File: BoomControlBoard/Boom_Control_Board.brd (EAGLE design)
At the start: 82.5 x 50.8 mm, 44 parts, among them J1 Servo, J2 FTDI, U1 ATMEGA328P, U2 3.3V/150mA, Y1 16MHz

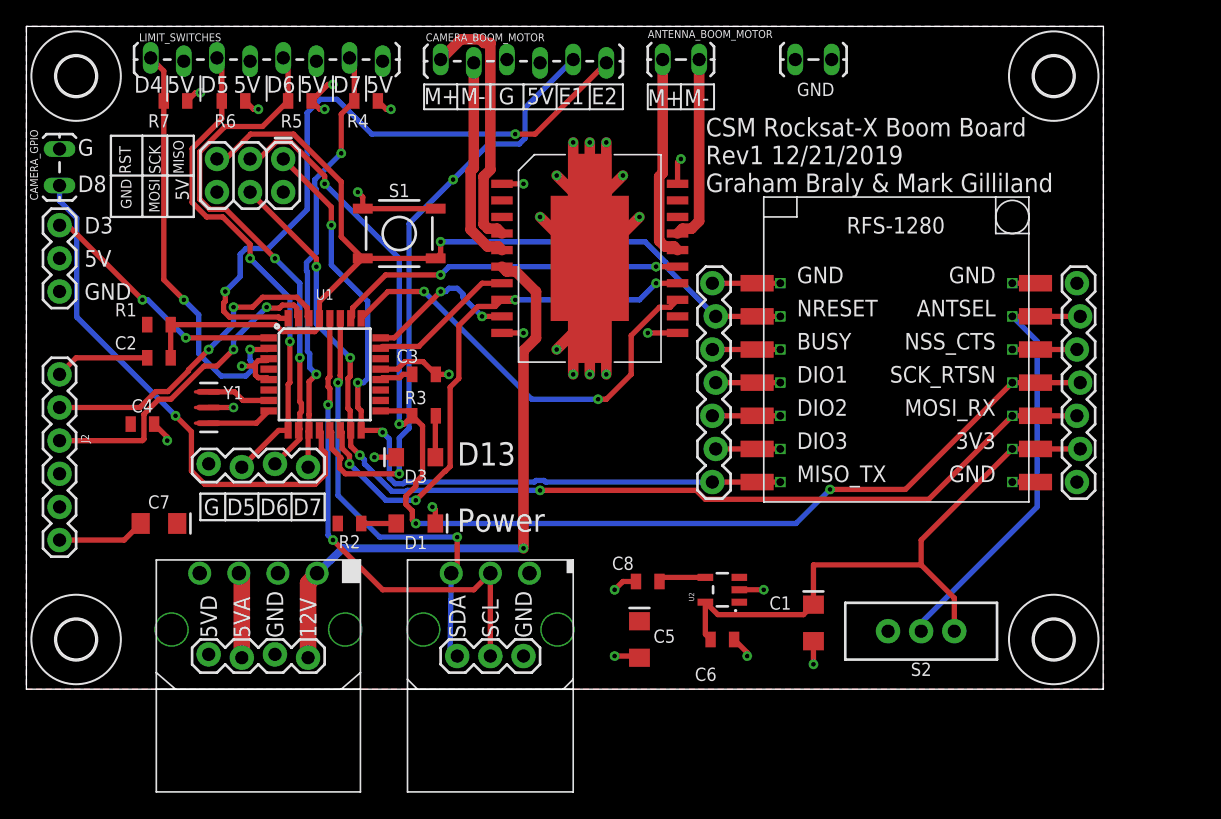
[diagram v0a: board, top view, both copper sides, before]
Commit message: Initial Rev2 for Boom and Exp. Control boards
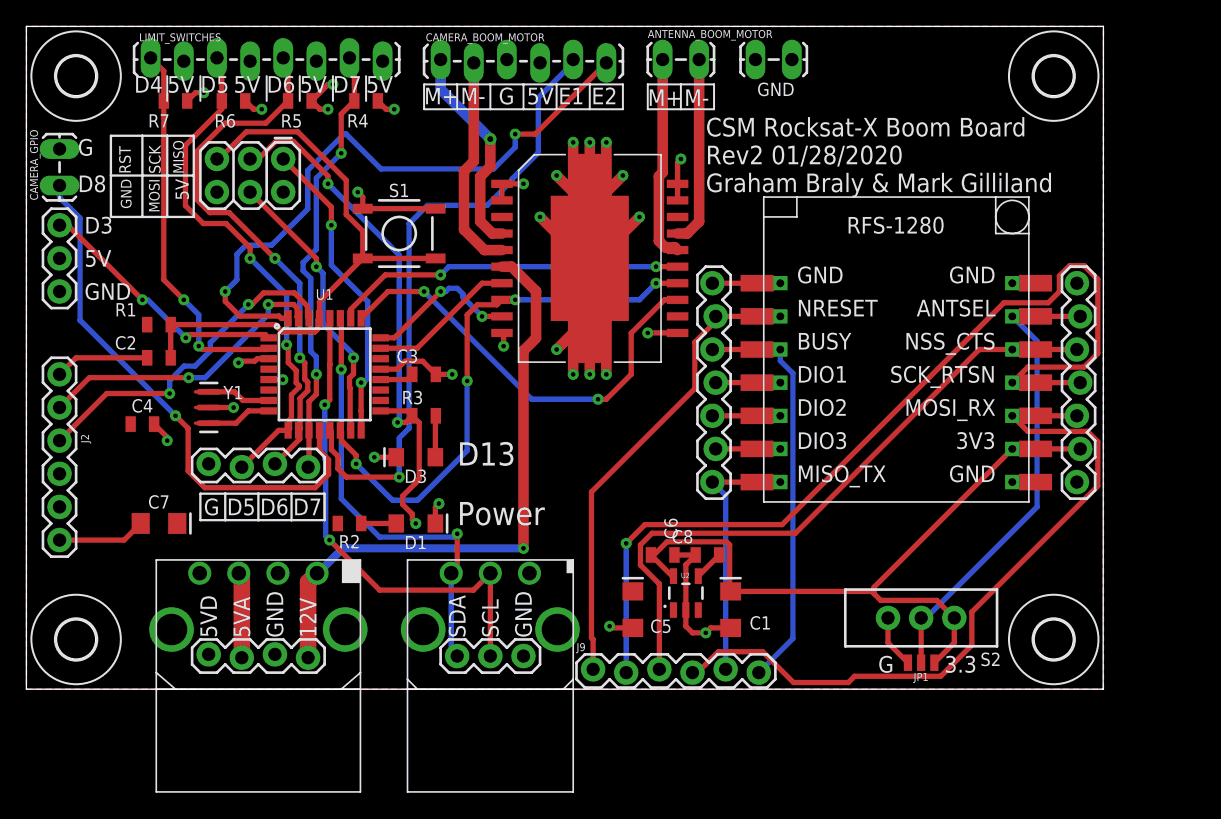
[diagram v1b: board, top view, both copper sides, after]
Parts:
- added J9: (no value), SparkFun-Connectors:1X06_LOCK
- added JP1: JUMPER-SMT_3_NO_NO_SILK, SparkFun-Jumpers:SMT-JUMPER_3_0-NO_TRACE_NO-SILK
- R2, R3: value 1kΩ -> 2.2kΩ
- moved C6 7.93 mm to (48.8, 10.3)
- moved C1 6.43 mm to (54.0, 6.10)
- moved C8 5.00 mm to (52.2, 10.3)
- moved GND 3.05 mm to (56.0, 48.3)
- moved U2 2.81 mm to (50.5, 7.37), turned to 0 degrees
- moved C5 2.34 mm to (46.5, 6.10)
- moved S2 1.02 mm to (68.6, 5.46)
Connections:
- removed net CTS: J5.5, U$5.P$12, U$5.P$26
- removed net N$6: J2.CTS
- new net RF_CTS: J5.5, J9.3, U$5.P$12, U$5.P$26
- new net RF_MISO: J4.1, J9.5, U$5.P$21, U$5.P$7
- new net RF_MOSI: J5.3, J9.4, U$5.P$10, U$5.P$24
- new net RF_RESET: J4.6, J9.1, U$5.P$16, U$5.P$2
- new net RF_SCK: J5.4, J9.2, U$5.P$11, U$5.P$25
- net 3V3: now also JP1.3
- net ANTSEL: now also JP1.2
- net BUSY: now also J9.6
- net GND: now also J2.CTS, JP1.1, U$4.19, U$4.2
- net MISO: no longer J4.1, U$5.P$21, U$5.P$7
- net MOSI: no longer J5.3, U$5.P$10, U$5.P$24
- net RESET: no longer J4.6, U$5.P$16, U$5.P$2
- net RXI: now also J2.TXO; no longer J2.RXI
- net SCK: no longer J5.4, U$5.P$11, U$5.P$25
- net TXO: now also J2.RXI; no longer J2.TXO
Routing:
- net RF_SCK: track 0.00 -> 74.4 mm, vias 0 -> 1
- net MOSI: track 83.1 -> 21.7 mm, vias 4 -> 2
- net RF_MOSI: track 0.00 -> 56.2 mm
- net SCK: track 97.4 -> 42.2 mm, vias 4 -> 3
- net RF_CTS: track 0.00 -> 49.8 mm
- net MISO: track 59.9 -> 23.8 mm, vias 3 -> 2
- net RF_RESET: track 0.00 -> 36.0 mm
- net RESET: track 74.9 -> 45.4 mm, vias 1 -> 0
- net BUSY: track 5.21 -> 31.5 mm
- net RF_MISO: track 0.00 -> 20.0 mm
- net 3V3: track 46.4 -> 55.3 mm
- net GND: track 151.6 -> 158.8 mm, vias 32 -> 30
- net CTS: track 4.95 -> 0.00 mm
- net CAMERA_+: track 20.4 -> 16.4 mm, vias 0 -> 1
- net PD4: track 32.2 -> 29.1 mm
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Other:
- board text added: "3.3"
- board text added: "CSM Rocksat-X Boom Board Rev2 01/28/2020 Graham Braly & Mark Gilliland"
- board text removed: "CSM Rocksat-X Boom Board Rev1 12/21/2019 Graham Braly & Mark Gilliland"

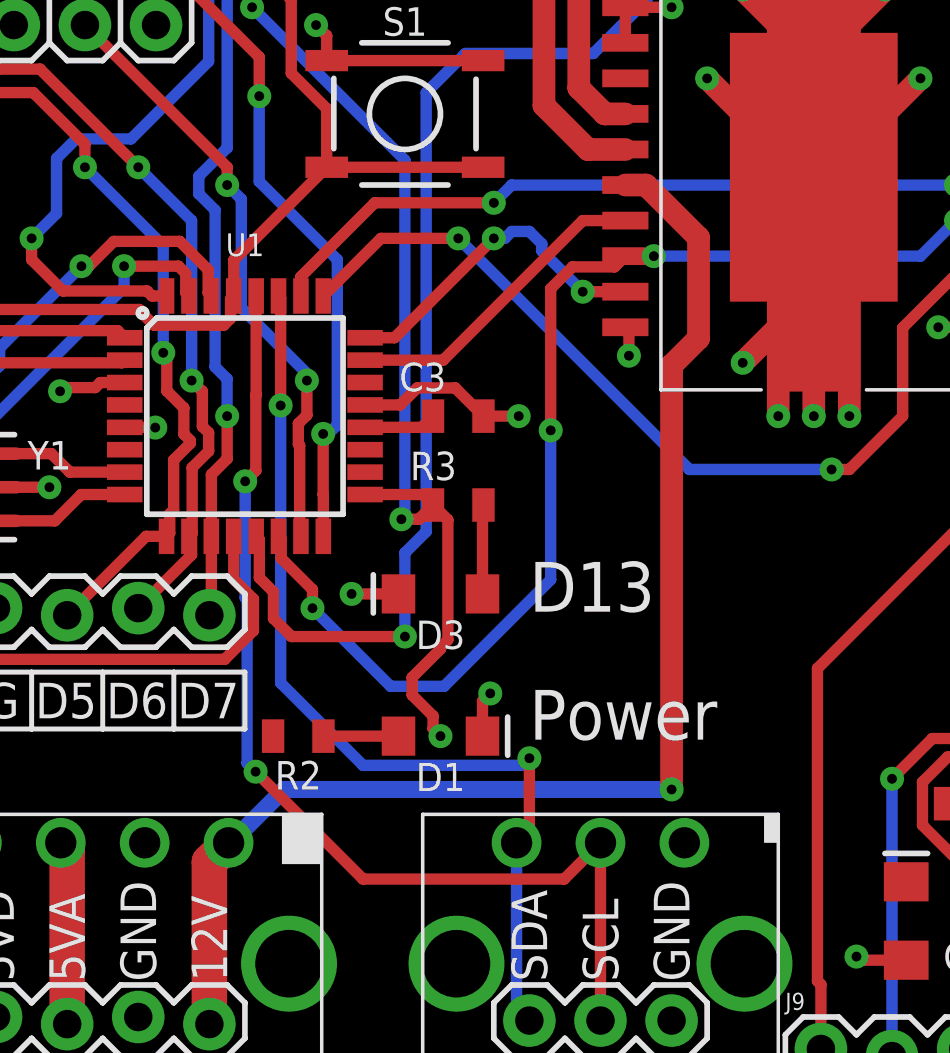
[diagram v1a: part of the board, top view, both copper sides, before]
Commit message: Minor improvements to Bomom and Exp. boards. Created safety switch board and switch footprint for MTA106
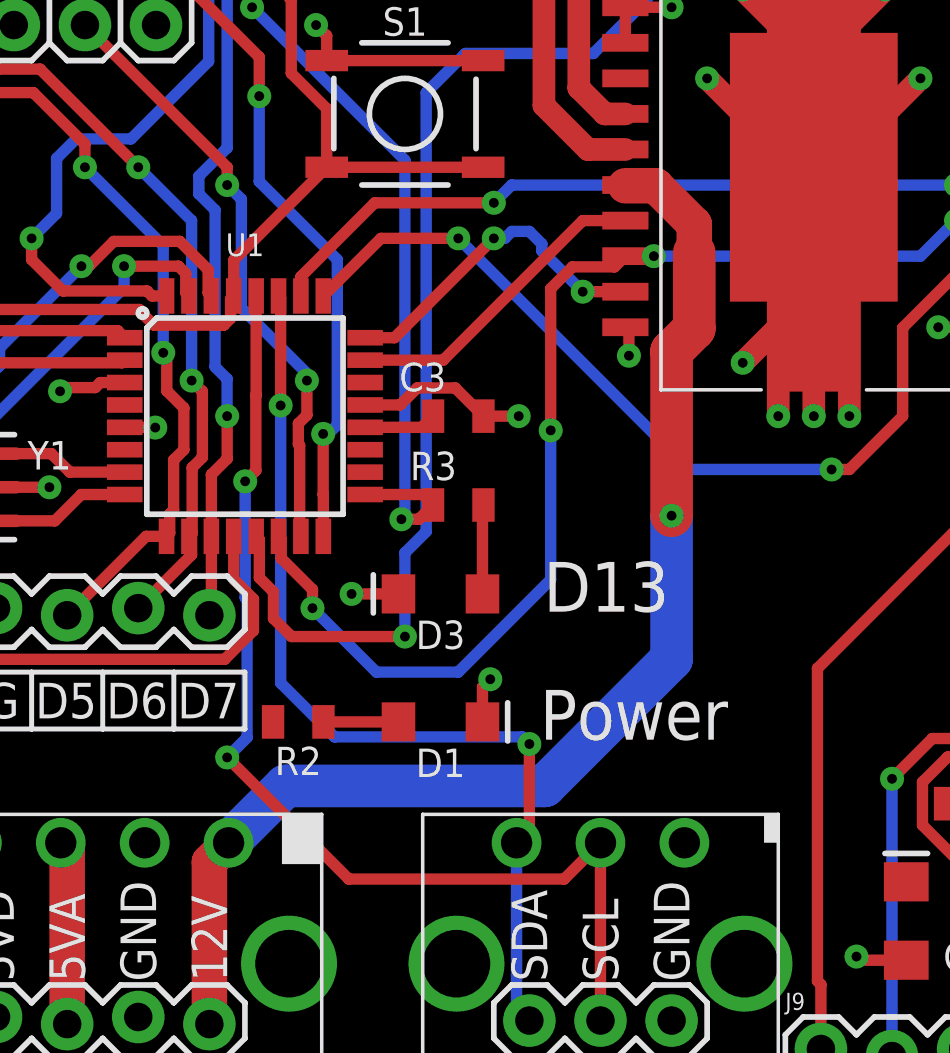
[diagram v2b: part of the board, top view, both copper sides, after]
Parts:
- moved D1 0.51 mm to (29.8, 13.2)
- moved R2 0.51 mm to (24.8, 13.2)
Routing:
- net SCK: track 42.2 -> 32.8 mm, vias 3 -> 2
- net 12V: track 46.9 -> 44.2 mm
- net SCL: track 38.1 -> 39.0 mm

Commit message: edits to exp and boom control boards
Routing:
- net GND: track 158.8 -> 163.4 mm
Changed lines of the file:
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@@
 </element>
 <element name="U2" library="SparkFun-IC-Power" package="SOT23-5" value="3.3V/150mA" x="50.546" y="7.366" smashed="yes">
-<attribute name="NAME" x="50.165" y="8.509" size="0.4064" layer="25"/>
+<attribute name="NAME" x="49.657" y="4.191" size="1.016" layer="25"/>
 <attribute name="PROD_ID" value="VREG-00822" x="50.546" y="7.366" size="1.778" layer="27" display="off"/>
 <attribute name="VALUE" x="49.5935" y="7.1755" size="0.4064" layer="27"/>
 </element>
 <element name="C6" library="SparkFun-Capacitors" package="0805" value="0.1uF" x="48.768" y="10.287" smashed="yes">
-<attribute name="NAME" x="48.895" y="12.319" size="1.016" layer="25" font="vector" ratio="20" rot="R270" align="bottom-center"/>
+<attribute name="NAME" x="47.625" y="12.573" size="1.016" layer="25" font="vector" ratio="20" align="bottom-center"/>
 <attribute name="PROD_ID" value="CAP-11624" x="48.768" y="10.287" size="1.778" layer="27" display="off"/>
-<attribute name="VALUE" x="47.625" y="13.208" size="1.016" layer="27" font="vector" ratio="20" rot="R90" align="top-center"/>
+<attribute name="VALUE" x="48.768" y="12.319" size="1.016" layer="27" font="vector" ratio="20" align="top-center"/>
 </element>
 <element name="S2" library="SparkFun-Switches" package="SWITCH_SPDT_PTH_11.6X4.0MM" value="ANTENNA_SELECT" x="68.58" y="5.461" smashed="yes" rot="R90">
@@
 </element>
 <element name="C1" library="SparkFun-Capacitors" package="EIA3216" value="10uF" x="53.975" y="6.096" smashed="yes" rot="R90">
-<attribute name="NAME" x="56.261" y="5.588" size="1.016" layer="25" font="vector" ratio="20" rot="R180" align="bottom-center"/>
+<attribute name="NAME" x="56.261" y="7.874" size="1.016" layer="25" font="vector" ratio="20" rot="R180" align="bottom-center"/>
 <attribute name="PROD_ID" value="CAP-00811" x="53.975" y="6.096" size="1.778" layer="27" rot="R90" display="off"/>
-<attribute name="VALUE" x="57.15" y="4.191" size="1.016" layer="27" font="vector" ratio="20" align="top-center"/>
+<attribute name="VALUE" x="57.15" y="6.477" size="1.016" layer="27" font="vector" ratio="20" align="top-center"/>
 </element>
 <element name="C5" library="SparkFun-Capacitors" package="EIA3216" value="10uF" x="46.482" y="6.096" smashed="yes" rot="R90">
-<attribute name="NAME" x="48.641" y="5.334" size="1.016" layer="25" font="vector" ratio="20" rot="R180" align="bottom-center"/>
+<attribute name="NAME" x="44.069" y="7.874" size="1.016" layer="25" font="vector" ratio="20" rot="R180" align="bottom-center"/>
 <attribute name="PROD_ID" value="CAP-00811" x="46.482" y="6.096" size="1.778" layer="27" rot="R90" display="off"/>
-<attribute name="VALUE" x="49.657" y="3.175" size="1.016" layer="27" font="vector" ratio="20" rot="R180" align="top-center"/>
+<attribute name="VALUE" x="43.815" y="5.715" size="1.016" layer="27" font="vector" ratio="20" rot="R180" align="top-center"/>
 </element>
 <element name="J3" library="SparkFun-Connectors" package="2X3" value="" x="19.685" y="40.64" smashed="yes" rot="R180">
@@
 </element>
 <element name="C8" library="SparkFun-Capacitors" package="0805" value="470pF" x="52.197" y="10.287" smashed="yes" rot="R180">
-<attribute name="NAME" x="50.292" y="11.176" size="1.016" layer="25" font="vector" ratio="20" align="bottom-center"/>
-<attribute name="VALUE" x="54.102" y="11.176" size="1.016" layer="27" font="vector" ratio="20" rot="R180" align="top-center"/>
+<attribute name="NAME" x="54.864" y="11.938" size="1.016" layer="25" font="vector" ratio="20" align="bottom-center"/>
+<attribute name="VALUE" x="56.134" y="10.668" size="1.016" layer="27" font="vector" ratio="20" rot="R180" align="top-center"/>
 </element>
 <element name="J4" library="SparkFun-Connectors" package="1X07_LOCK" value="" x="52.705" y="15.875" smashed="yes" rot="R90">
@@
 <wire x1="51.297" y1="10.287" x2="50.546" y2="9.536" width="0.4064" layer="1"/>
 <wire x1="50.546" y1="9.536" x2="50.546" y2="6.0659" width="0.4064" layer="1"/>
-<wire x1="28.345" y1="17.78" x2="31.623" y2="14.732" width="0" layer="19" extent="1-1"/>
+<wire x1="28.345" y1="17.78" x2="31.393" y2="14.732" width="0.4064" layer="1"/>
+<wire x1="31.393" y1="14.732" x2="31.623" y2="14.732" width="0.4064" layer="1"/>
 </signal>
 <signal name="DTR">
@@
 <contactref element="U$4" pad="14"/>
 <via x="25.273" y="17.2692" extent="1-16" drill="0.35"/>
-<wire x1="25.273" y1="17.2692" x2="27.5534" y2="14.9888" width="0.4064" layer="16"/>
+<wire x1="25.273" y1="17.2692" x2="27.8074" y2="14.7348" width="0.4064" layer="16"/>
 <wire x1="36.449" y1="29.845" x2="37.465" y2="29.845" width="0.4064" layer="1"/>
 <via x="37.465" y="29.845" extent="1-16" drill="0.35"/>
@@
 <wire x1="33.782" y1="18.288" x2="33.782" y2="23.622" width="0.4064" layer="16"/>
 <via x="33.782" y="23.622" extent="1-16" drill="0.35"/>
-<wire x1="27.5534" y1="14.9888" x2="30.4828" y2="14.9888" width="0.4064" layer="16"/>
-<wire x1="30.4828" y1="14.9888" x2="33.782" y2="18.288" width="0.4064" layer="16"/>
-<wire x1="36.0652" y1="29.4612" x2="36.449" y2="29.845" width="0.4064" layer="1"/>
-<wire x1="34.55791875" y1="29.4612" x2="36.0652" y2="29.4612" width="0.4064" layer="1"/>
+<wire x1="27.8074" y1="14.7348" x2="30.2288" y2="14.7348" width="0.4064" layer="16"/>
+<wire x1="30.2288" y1="14.7348" x2="33.782" y2="18.288" width="0.4064" layer="16"/>
 <wire x1="33.782" y1="23.622" x2="33.782" y2="28.68528125" width="0.4064" layer="1"/>
-<wire x1="33.782" y1="28.68528125" x2="34.55791875" y2="29.4612" width="0.4064" layer="1"/>
+<wire x1="34.94171875" y1="29.845" x2="36.449" y2="29.845" width="0.4064" layer="1"/>
+<wire x1="33.782" y1="28.68528125" x2="34.94171875" y2="29.845" width="0.4064" layer="1"/>
 </signal>
 <signal name="N$5">
